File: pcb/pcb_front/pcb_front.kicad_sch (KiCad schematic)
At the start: 24 parts, among them J1 MicroLab, J2 LED_BREAKOUT, J3 GAS_BREAKOUT, U1 TBD62783A

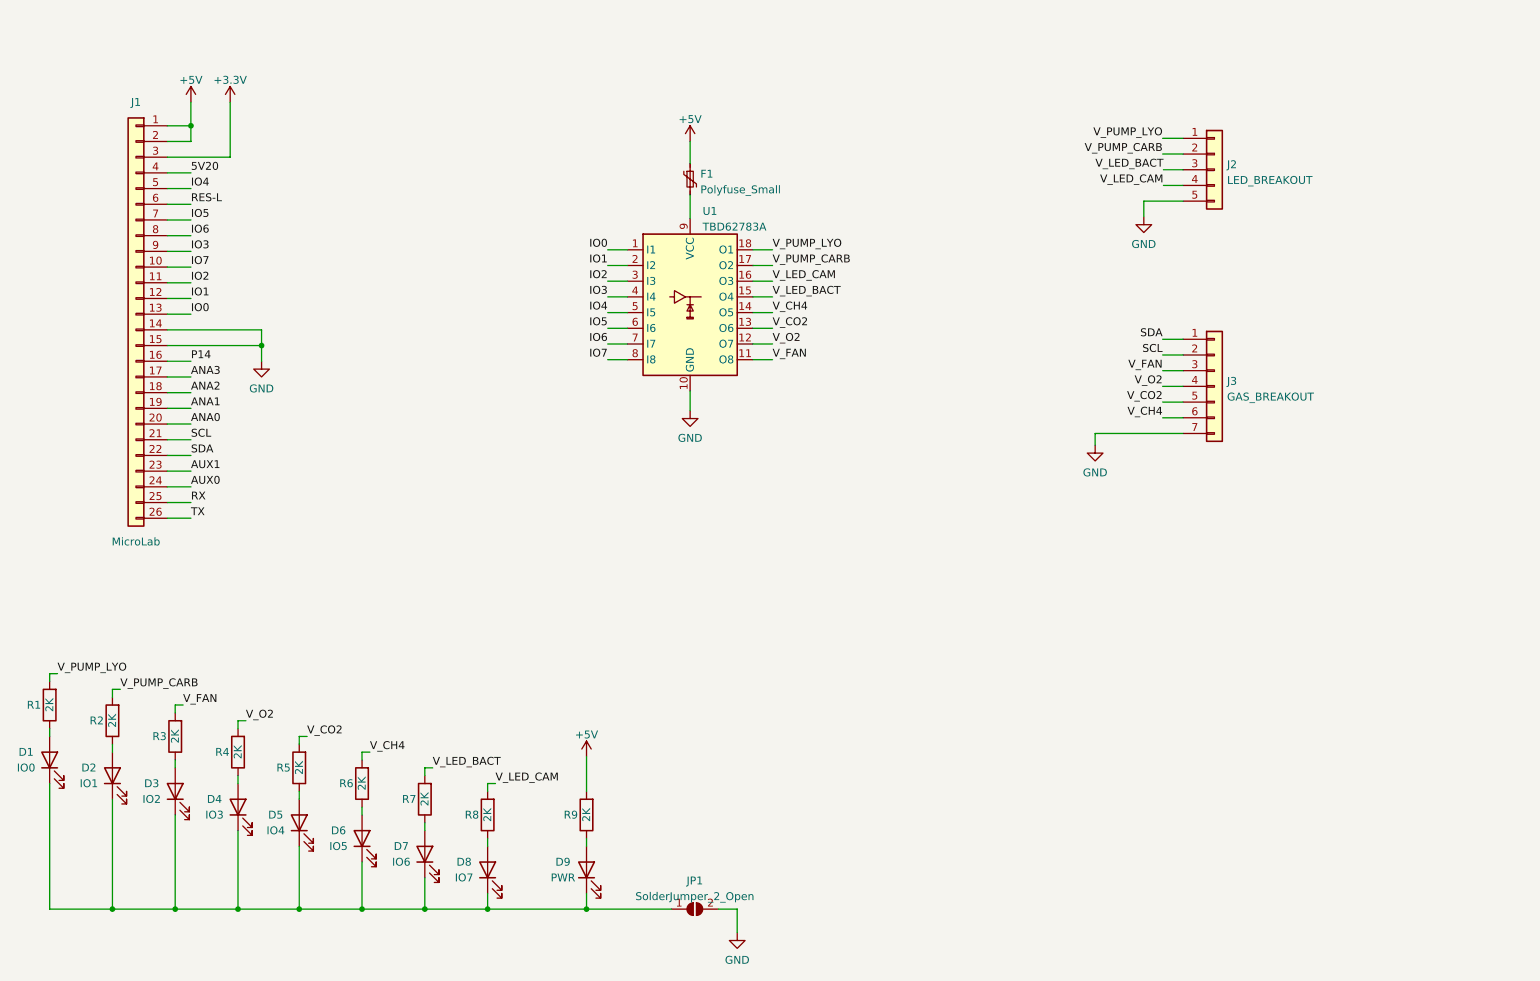
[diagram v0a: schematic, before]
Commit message: curved gnd plane on corners
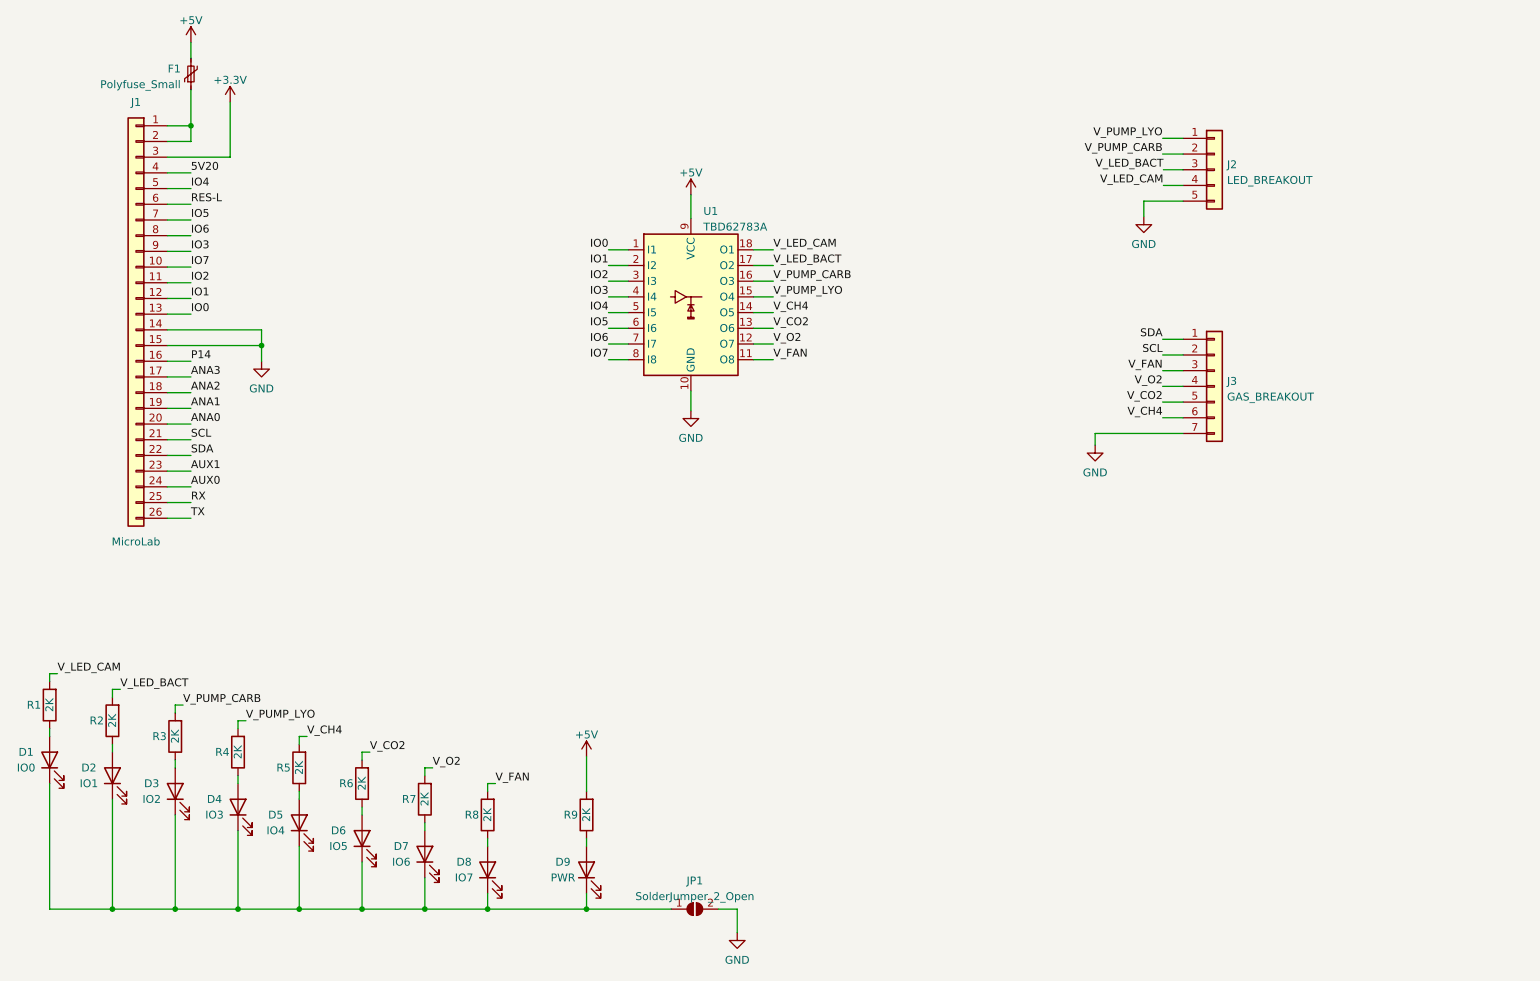
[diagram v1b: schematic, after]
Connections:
- net +5V: now also F1.2, U1.9 (VCC); no longer F1.1, J1.1 (Pin_1), J1.2 (Pin_2)
- net V_CH4: now also R5.2; no longer R6.2
- net V_CO2: now also R6.2; no longer R5.2
- net V_FAN: now also R8.2; no longer R3.2
- net V_LED_BACT: now also R2.2, U1.17 (O2); no longer R7.2, U1.15 (O4)
- net V_LED_CAM: now also R1.2, U1.18 (O1); no longer R8.2, U1.16 (O3)
- net V_O2: now also R7.2; no longer R4.2
- net V_PUMP_CARB: now also R3.2, U1.16 (O3); no longer R2.2, U1.17 (O2)
- net V_PUMP_LYO: now also R4.2, U1.15 (O4); no longer R1.2, U1.18 (O1)
- new net: F1.1, J1.1 (Pin_1), J1.2 (Pin_2)
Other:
- moved on the sheet: F1

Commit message: front pcb rev 2
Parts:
- removed D2: IO1, LED_SMD:LED_0603_1608Metric, symbol Device:LED
- removed D3: IO2, LED_SMD:LED_0603_1608Metric, symbol Device:LED
- removed D4: IO3, LED_SMD:LED_0603_1608Metric, symbol Device:LED
- removed D5: IO4, LED_SMD:LED_0603_1608Metric, symbol Device:LED
- removed D6: IO5, LED_SMD:LED_0603_1608Metric, symbol Device:LED
- removed D7: IO6, LED_SMD:LED_0603_1608Metric, symbol Device:LED
- removed D8: IO7, LED_SMD:LED_0603_1608Metric, symbol Device:LED
- removed D9: PWR, LED_SMD:LED_0603_1608Metric, symbol Device:LED
- removed F1: Polyfuse_Small, Fuse:Fuse_0603_1608Metric, symbol Device:Polyfuse_Small
- removed J1: MicroLab, Connector_PinSocket_2.00mm:PinSocket_2x13_P2.00mm_Horizontal, symbol Connector_Generic:Conn_01x26
- removed J2: LED_BREAKOUT, Connector_JST:JST_SH_SM05B-SRSS-TB_1x05-1MP_P1.00mm_Horizontal, symbol Connector_Generic:Conn_01x05
- removed J3: GAS_BREAKOUT, Connector_JST:JST_SH_SM07B-SRSS-TB_1x07-1MP_P1.00mm_Horizontal, symbol Connector_Generic:Conn_01x07
- removed JP1: SolderJumper_2_Open, Jumper:SolderJumper-2_P1.3mm_Open_TrianglePad1.0x1.5mm, symbol Jumper:SolderJumper_2_Open
- removed R1, R2, R3, R4, R5, R6, R7, R8, R9: 2K, Resistor_SMD:R_0603_1608Metric, symbol Device:R
- removed U1: TBD62783A, Package_DIP:DIP-18_W7.62mm_Socket, symbol Transistor_Array:TBD62783A
- added H1, H2, H3: M2, MountingHole:MountingHole_2.2mm_M2_DIN965_Pad, symbol Mechanical:MountingHole_Pad
- added J1: MicroLab, Connector_PinHeader_2.00mm:PinHeader_2x13_P2.00mm_Vertical, symbol Connector_Generic:Conn_02x13_Odd_Even
- added J2: Gas Breakout, Connector_JST:JST_SH_BM08B-SRSS-TB_1x08-1MP_P1.00mm_Vertical, symbol Connector_Generic_MountingPin:Conn_01x08_MountingPin
- added J3: LED Breakout, Connector_JST:JST_SH_BM05B-SRSS-TB_1x05-1MP_P1.00mm_Vertical, symbol Connector_Generic_MountingPin:Conn_01x05_MountingPin
- added R1: 2K, Resistor_SMD:R_0402_1005Metric_Pad0.72x0.64mm_HandSolder, symbol Device:R_Small
- D1: value IO0 -> LED; footprint LED_SMD:LED_0603_1608Metric -> LED_SMD:LED_0402_1005Metric_Pad0.77x0.64mm_HandSolder
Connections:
- net +3.3V: now also J1.3 (Pin_3)
- net +5V: now also J1.1 (Pin_1), J1.2 (Pin_2), J2.1 (Pin_1), J3.1 (Pin_1), R1.2
- net 5V20: now also J1.4 (Pin_4)
- net ANA0: now also J1.20 (Pin_20)
- net ANA1: now also J1.19 (Pin_19)
- net ANA2: now also J1.18 (Pin_18)
- net ANA3: now also J1.17 (Pin_17)
- net AUX0: now also J1.24 (Pin_24)
- net AUX1: now also J1.23 (Pin_23)
- net GND: now also D1.1 (K), H1.1, H2.1, H3.1, J1.14 (Pin_14), J1.15 (Pin_15), J2.8 (Pin_8), J2.MP (MountPin), J3.5 (Pin_5), J3.MP (MountPin)
- net IO0: now also J1.13 (Pin_13), J3.2 (Pin_2)
- net IO1: now also J1.12 (Pin_12), J3.3 (Pin_3)
- net IO2: now also J1.11 (Pin_11), J3.4 (Pin_4)
- net IO3: now also J1.9 (Pin_9), J2.5 (Pin_5)
- net IO4: now also J1.5 (Pin_5), J2.2 (Pin_2)
- net IO5: now also J1.7 (Pin_7), J2.3 (Pin_3)
- net IO6: now also J1.8 (Pin_8), J2.4 (Pin_4)
- net IO7: now also J1.10 (Pin_10)
- net P14: now also J1.16 (Pin_16)
- net RES-L: now also J1.6 (Pin_6)
- net RX: now also J1.25 (Pin_25)
- net SCL: now also J1.21 (Pin_21), J2.7 (Pin_7)
- net SDA: now also J1.22 (Pin_22), J2.6 (Pin_6)
- net TX: now also J1.26 (Pin_26)
- net at D1.2 (A): now also R1.1

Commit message: front pcb rev 2
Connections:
- net IO0: now also J3.4 (Pin_4); no longer J3.2 (Pin_2)
- net IO2: now also J3.2 (Pin_2); no longer J3.4 (Pin_4)
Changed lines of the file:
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@@
     (effects (font (size 1.27 1.27)) (justify right bottom))
   )
-  (label "IO2" (at 198.12 96.52 180)
+  (label "IO2" (at 198.12 91.44 180)
     (effects (font (size 1.27 1.27)) (justify right bottom))
   )
@@
     (effects (font (size 1.27 1.27)) (justify right bottom))
   )
-  (label "IO0" (at 198.12 91.44 180)
+  (label "IO0" (at 198.12 96.52 180)
     (effects (font (size 1.27 1.27)) (justify right bottom))
   )

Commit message: fin
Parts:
- removed J2: Gas Breakout, Connector_JST:JST_SH_BM08B-SRSS-TB_1x08-1MP_P1.00mm_Vertical, symbol Connector_Generic_MountingPin:Conn_01x08_MountingPin
- added J2: Sensors, Connector_JST:JST_SH_BM04B-SRSS-TB_1x04-1MP_P1.00mm_Vertical, symbol Connector_Generic_MountingPin:Conn_01x04_MountingPin
- J3: value LED Breakout -> LED
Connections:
- net +5V: now also J2.1 (Pin_1)
- net GND: now also J2.4 (Pin_4), J2.MP (MountPin)
- net IO1: no longer J3.3 (Pin_3)
- net IO2: now also J3.3 (Pin_3); no longer J3.2 (Pin_2)
- net IO3: now also J3.2 (Pin_2)
- net SCL: now also J2.3 (Pin_3)
- net SDA: now also J2.2 (Pin_2)

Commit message: production ver. of PCB
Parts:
- removed J3: LED, Connector_JST:JST_SH_BM05B-SRSS-TB_1x05-1MP_P1.00mm_Vertical, symbol Connector_Generic_MountingPin:Conn_01x05_MountingPin
- added D2, D3, D4: D_Small, Diode_SMD:D_SOD-323, symbol Device:D_Small
- added H4: M2, MountingHole:MountingHole_2.2mm_M2_DIN965_Pad, symbol Mechanical:MountingHole_Pad
- added J3: Pump 1, Connector_JST:JST_SH_BM02B-SRSS-TB_1x02-1MP_P1.00mm_Vertical, symbol Connector_Generic_MountingPin:Conn_01x02_MountingPin
- added J4: Pump 2, Connector_JST:JST_SH_BM02B-SRSS-TB_1x02-1MP_P1.00mm_Vertical, symbol Connector_Generic_MountingPin:Conn_01x02_MountingPin
- added J5: LED, Connector_JST:JST_SH_BM02B-SRSS-TB_1x02-1MP_P1.00mm_Vertical, symbol Connector_Generic_MountingPin:Conn_01x02_MountingPin
- added Q1, Q2, Q3: NX7002BKR, SOT95P230X110-3N, symbol Mouser Parts:NX7002BKR
- added R2, R3, R4: 10K, Resistor_SMD:R_0402_1005Metric, symbol Device:R_Small
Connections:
- net +5V: now also D2.1 (K), D3.1 (K), D4.1 (K), J3.1 (Pin_1), J4.1 (Pin_1), J5.1 (Pin_1)
- net GND: now also H4.1, J3.MP (MountPin), J4.MP (MountPin), J5.MP (MountPin), Q1.2, Q2.2, Q3.2, R2.2, R3.2, R4.2
- net IO3: now also Q1.1, R2.1
- net IO4: now also Q3.1, R4.1
- net IO5: now also Q2.1, R3.1
- new net: D4.2 (A), J5.2 (Pin_2), Q3.3
- new net: D3.2 (A), J4.2 (Pin_2), Q2.3
- new net: D2.2 (A), J3.2 (Pin_2), Q1.3
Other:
- moved on the sheet: D1, H1, H2, H3, J1, J2, R1
